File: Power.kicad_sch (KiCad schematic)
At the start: 52 parts, among them U1 STHW4-DU-HN050206, U3 TPS546D24SRVFR, U4 TPS62933DRLR, U5 TPS62933DRLR

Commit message: AI BOM updates
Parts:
- C12, C8: LCSC C15850 -> C344022
- C15: LCSC C52923 -> C2177690
- C22: DK (none) -> 490-GRM21BR60J476ME01KCT-ND; LCSC C45783 -> C16780; PARTNO MSASJ21GBB5476MTNA01 -> GRM21BR60J476ME01K
- C35, C36: LCSC C45783 -> C29277

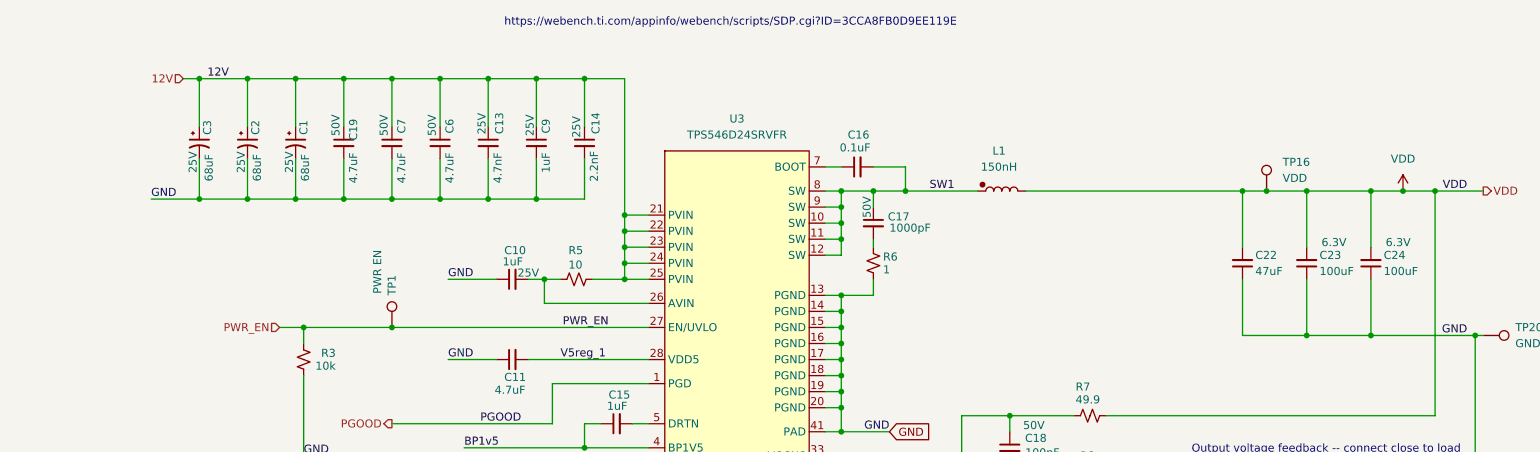
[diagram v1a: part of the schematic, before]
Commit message: first pass DFM
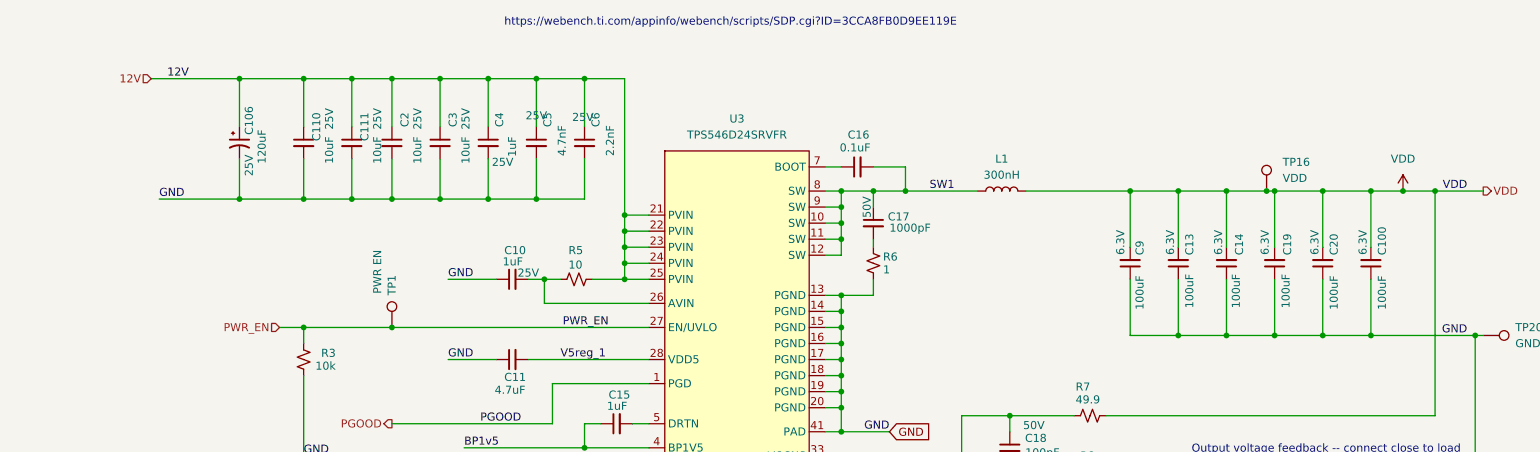
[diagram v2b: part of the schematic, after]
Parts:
- removed C1, C2, C3: 68uF, Capacitor_SMD:CP_Elec_5x5.8, symbol Device:C_Polarized_Small_US
- removed C22: 47uF, Capacitor_SMD:C_0805_2012Metric, symbol Device:C_Small
- removed C23, C24: 100uF, Capacitor_SMD:C_1210_3225Metric, symbol Device:C_Small
- removed C7: 4.7uF, Capacitor_SMD:C_1206_3216Metric, symbol Device:C_Small
- removed L1: 150nH, bitaxe:GDIM107050-R15S1MTF-0R37, symbol bitaxe:L-polarized
- added C100, C20: 100uF, Capacitor_SMD:C_1206_3216Metric, symbol Device:C_Small
- added C106: 120uF, Capacitor_SMD:CP_Elec_6.3x5.9, symbol Device:C_Polarized_Small_US
- added C110, C111, C2, C3: 10uF, Capacitor_SMD:C_0603_1608Metric, symbol Device:C_Small
- added C4: 1uF, Capacitor_SMD:C_0402_1005Metric, symbol Device:C_Small
- added C5: 4.7nF, Capacitor_SMD:C_0402_1005Metric, symbol Device:C_Small
- added L1: 300nH, bitaxe:SLC1175-271MEC_COC, symbol Device:L
- C13: value 4.7nF -> 100uF; footprint Capacitor_SMD:C_0402_1005Metric -> Capacitor_SMD:C_1206_3216Metric; DK 490-1309-1-ND -> 1276-1782-1-ND; PARTNO GRM155R71E472KA01D -> CL31A107MQHNNNE; Voltage 25V -> 6.3V
- C14: value 2.2nF -> 100uF; footprint Capacitor_SMD:C_0402_1005Metric -> Capacitor_SMD:C_1206_3216Metric; DK 490-8257-1-ND -> 1276-1782-1-ND; PARTNO GRM155R61H222KA01D -> CL31A107MQHNNNE; Voltage 25V -> 6.3V
- C19: value 4.7uF -> 100uF; DK 490-6521-1-ND -> 1276-1782-1-ND; PARTNO GRM31CR71H475KA12L -> CL31A107MQHNNNE; Voltage 50V -> 6.3V
- C6: value 4.7uF -> 2.2nF; footprint Capacitor_SMD:C_1206_3216Metric -> Capacitor_SMD:C_0402_1005Metric; DK 490-6521-1-ND -> 490-8257-1-ND; PARTNO GRM31CR71H475KA12L -> GRM155R61H222KA01D; Voltage 50V -> 25V
- C9: value 1uF -> 100uF; footprint Capacitor_SMD:C_0603_1608Metric -> Capacitor_SMD:C_1206_3216Metric; DK 1276-1184-1-ND -> 1276-1782-1-ND; PARTNO CL10B105KA8NNNC -> CL31A107MQHNNNE; Voltage 25V -> 6.3V
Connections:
- net 12V: now also C106.1, C110.1, C111.1, C2.1, C3.1, C4.1, C5.1; no longer C13.1, C14.1, C19.1, C9.1
- net GND: now also C13.1, C14.1, C19.1, C9.1, C100.1, C106.2, C110.2, C111.2, C2.2, C20.1, C3.2, C4.2, C5.2; no longer C13.2, C14.2, C19.2, C9.2
- net SW1: now also L1.1
- net VDD: now also C13.2, C14.2, C19.2, C9.2, C100.2, C20.2, L1.2

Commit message: AGND and OSNS
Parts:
- removed C10: 1uF, Capacitor_SMD:C_0603_1608Metric, symbol Device:C_Small
- added C21: 1uF, Capacitor_SMD:C_0402_1005Metric, symbol Device:C_Small
- added NT2: NetTie_1, bitaxe:NetTie-2_SMD_Pad0.2mmx1mm, symbol Device:NetTie_2
- added NT5, NT6: NetTie_2, bitaxe:NetTie-2_SMD_Pad0.2mmx1mm, symbol Device:NetTie_2
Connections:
- net GND: now also NT2.1, NT6.2; no longer R8.2, U3.37 (AGND)
- net VDD: now also NT5.2; no longer R7.1
- net at R5.2, U3.26 (AVIN): now also C21.2
- new net AGND: C21.1, NT2.2, U3.37 (AGND)
- new net OSNS+: NT5.1, R7.1
- new net OSNS-: NT6.1, R8.2

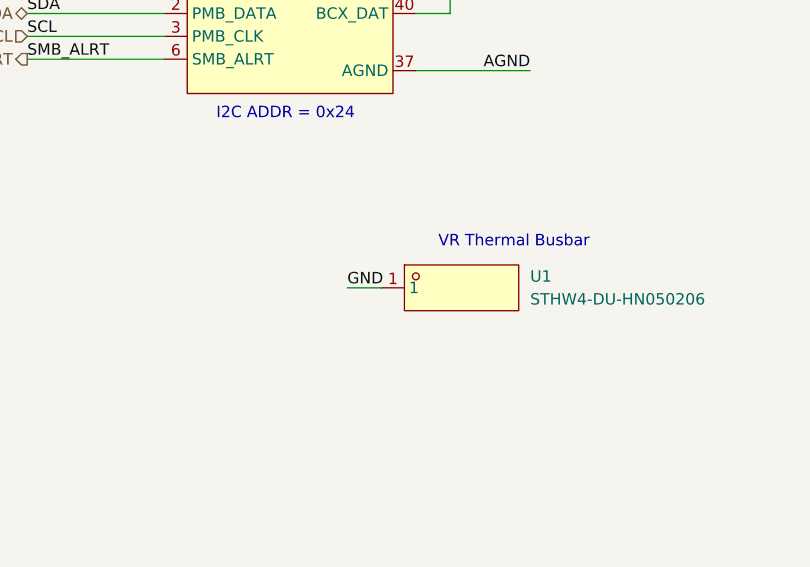
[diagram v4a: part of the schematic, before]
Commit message: footprint, BOM cleanup. bypass capacitor spacing cleanup
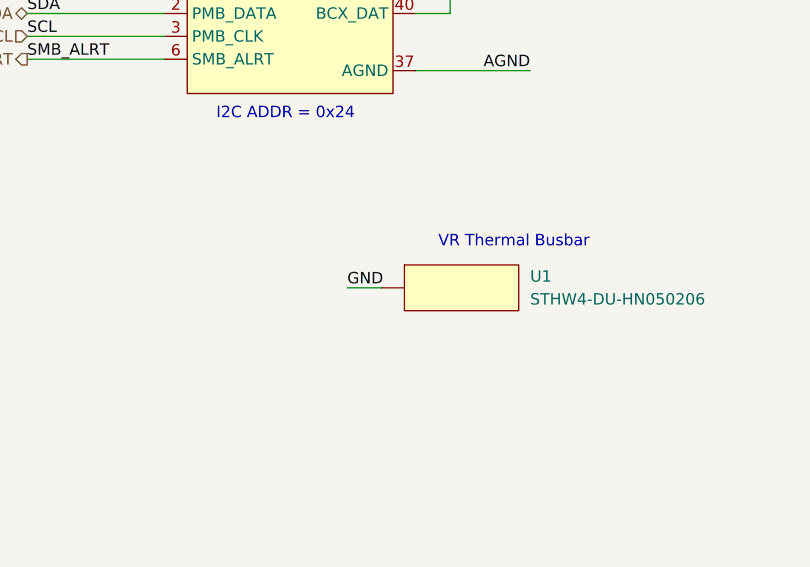
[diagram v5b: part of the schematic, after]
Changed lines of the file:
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@@
 		)
 		(property "LCSC" "C18548300"
-			(at 233.68 158.75 0)
+			(at 236.474 168.91 0)
 			(hide yes)
 			(show_name no)
@@
 			)
 		)
-		(property "Datasheet" "https://products.sumida.com/products/pdf/104CDMCCDS.pdf"
+		(property "Datasheet" "https://www.coilcraft.com/getmedia/59efd6f6-bdf3-4b2c-9ea4-f86f22cfee4e/slc1175.pdf"
 			(at 260.35 66.04 0)
 			(hide yes)

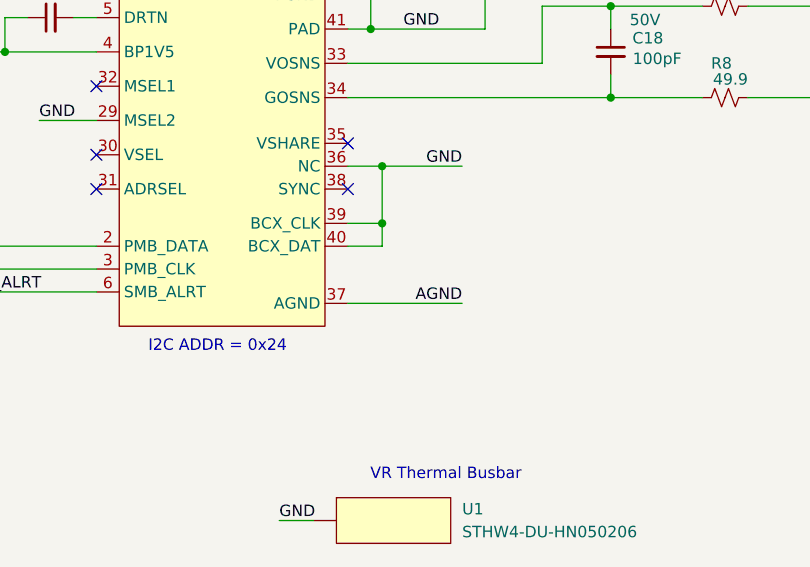
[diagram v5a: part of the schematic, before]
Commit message: fix all DRC and ERC
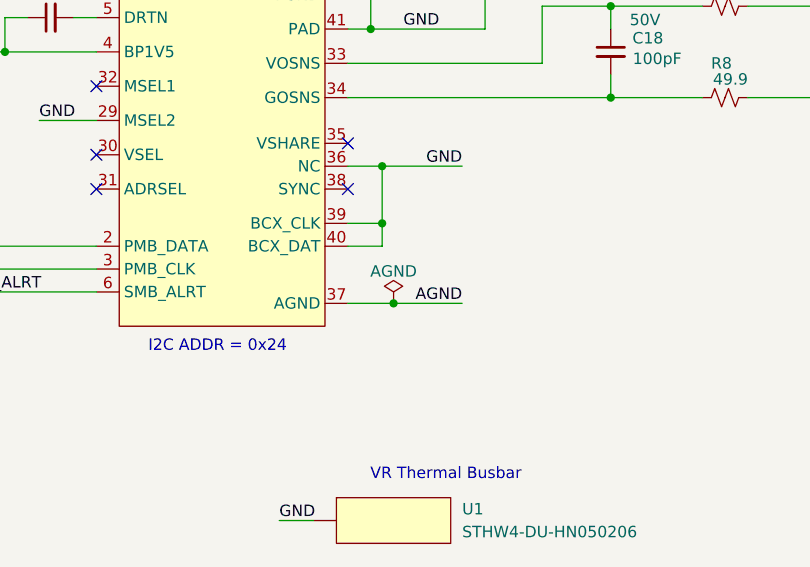
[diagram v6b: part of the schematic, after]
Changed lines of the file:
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@@
 	)
 	(junction
+		(at 237.49 134.62)
+		(diameter 0)
+		(color 0 0 0 0)
+	)
+	(junction
 		(at 234.95 95.25)
 		(diameter 0)
@@
 	(wire
 		(pts
+			(xy 237.49 134.62) (xy 245.11 134.62)
+		)
+		(stroke
+			(width 0)
+			(type default)
+		)
+	)
+	(wire
+		(pts
 			(xy 100.33 189.23) (xy 105.41 189.23)
 		)
@@
 	(wire
 		(pts
-			(xy 232.41 134.62) (xy 245.11 134.62)
+			(xy 232.41 134.62) (xy 237.49 134.62)
 		)
 		(stroke
@@
 					(unit 1)
 				)
+			)
+		)
+	)
+	(symbol
+		(lib_id "power:PWR_FLAG")
+		(at 237.49 134.62 0)
+		(unit 1)
+		(body_style 1)
+		(exclude_from_sim no)
+		(in_bom yes)
+		(on_board yes)
+		(in_pos_files yes)
+		(dnp no)
+		(property "Reference" "#FLG02"
+			(at 237.49 132.715 0)
+			(hide yes)
+			(show_name no)
+			(do_not_autoplace no)
+			(effects
+				(font
+					(size 1.27 1.27)
+				)
+			)
+		)
+		(property "Value" "AGND"
+			(at 237.49 131.064 0)
+			(show_name no)
+			(do_not_autoplace no)
+			(effects
+				(font
+					(size 1.27 1.27)
+				)
+			)
+		)
+		(property "Footprint" ""
+			(at 237.49 134.62 0)
+			(hide yes)
+			(show_name no)
+			(do_not_autoplace no)
+			(effects
+				(font
+					(size 1.27 1.27)
+				)
+			)
+		)
+		(property "Datasheet" ""
+			(at 237.49 134.62 0)
+			(hide yes)
+			(show_name no)
+			(do_not_autoplace no)
+			(effects
+				(font
+					(size 1.27 1.27)
+				)
+			)
+		)
+		(property "Description" "Special symbol for telling ERC where power comes from"
+			(at 237.49 134.62 0)
+			(hide yes)
+			(show_name no)
+			(do_not_autoplace no)
+			(effects
+				(font
+					(size 1.27 1.27)
+				)
+			)
+		)
+		(pin "1"
+		)
+		(instances
+			(project "bitaxeNaja"
+				(path "/61fe8d2c-9301-4ad9-8caf-c47acfa835b0/24036843-8461-4d4b-b738-f953c909ed6c"
+					(reference "#FLG02")
+					(unit 1)
+				)

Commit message: moved the 3V3 level shifter down out of the main GND power plane. BOM cleanup
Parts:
- C110, C111, C2, C3: LCSC (none) -> C344022

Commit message: remove malformed fields in schematic
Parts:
- C42, C43: Manufacturer Murata Electronics -> (none)
